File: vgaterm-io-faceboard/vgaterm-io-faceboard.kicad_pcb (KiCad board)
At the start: 2 copper layers, 37.6 x 19.1 mm, 8 parts, among them J1 Conn_01x02, J2 USB_B_Micro UART, J3 Conn_01x04, J4 Conn_01x04

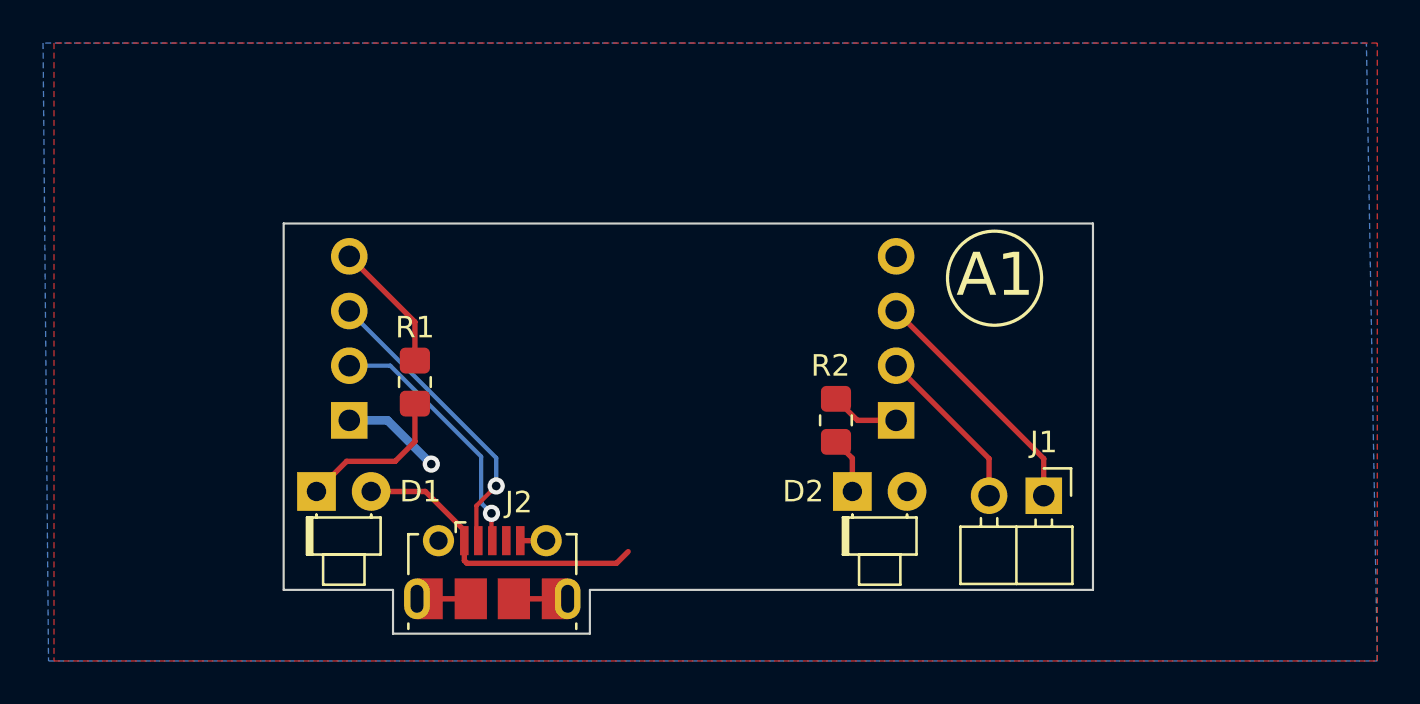
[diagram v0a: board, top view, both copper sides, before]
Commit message: updating timing board hsync vsync delay
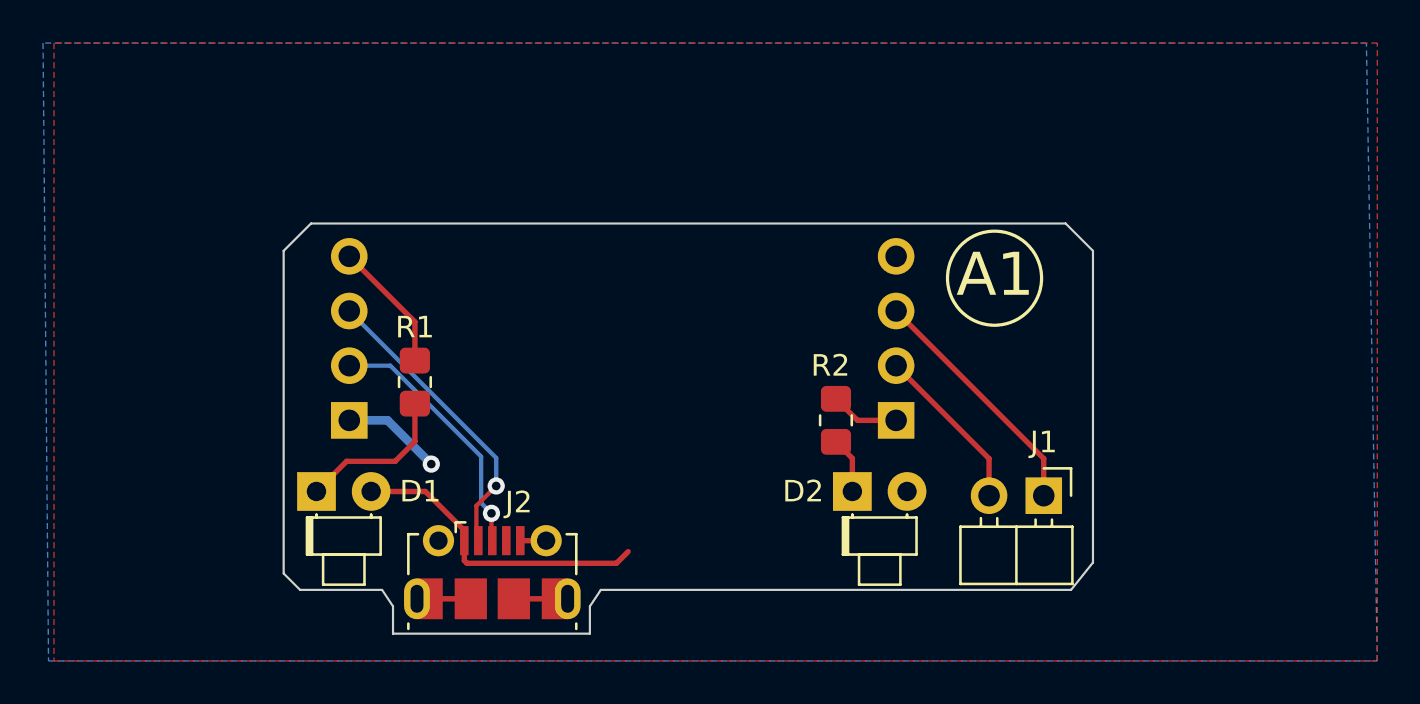
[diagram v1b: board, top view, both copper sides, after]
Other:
- outline, holes or cut-outs redrawn
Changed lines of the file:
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@@
   (gr_line (start 91.186 80.01) (end 82.042 80.01)
     (stroke (width 0.1) (type default)) (layer "Edge.Cuts"))
-  (gr_line (start 82.042 80.01) (end 82.042 77.978)
+  (gr_line (start 76.962 62.23) (end 78.232 60.96)
     (stroke (width 0.1) (type default)) (layer "Edge.Cuts"))
-  (gr_line (start 82.042 77.978) (end 76.962 77.978)
+  (gr_line (start 114.554 62.23) (end 113.284 60.96)
     (stroke (width 0.1) (type default)) (layer "Edge.Cuts"))
-  (gr_line (start 114.554 60.96) (end 114.554 77.978)
+  (gr_line (start 82.042 80.01) (end 82.042 78.74)
     (stroke (width 0.1) (type default)) (layer "Edge.Cuts"))
-  (gr_line (start 76.962 77.978) (end 76.962 60.96)
+  (gr_line (start 91.186 78.74) (end 91.694 77.978)
     (stroke (width 0.1) (type default)) (layer "Edge.Cuts"))
-  (gr_line (start 91.186 77.978) (end 91.186 80.01)
+  (gr_line (start 81.534 77.978) (end 82.042 78.74)
     (stroke (width 0.1) (type default)) (layer "Edge.Cuts"))
-  (gr_line (start 114.554 77.978) (end 91.186 77.978)
+  (gr_line (start 81.534 77.978) (end 77.724 77.978)
     (stroke (width 0.1) (type default)) (layer "Edge.Cuts"))
-  (gr_line (start 76.962 60.96) (end 114.554 60.96)
+  (gr_line (start 77.724 77.978) (end 76.962 77.216)
+    (stroke (width 0.1) (type default)) (layer "Edge.Cuts"))
+  (gr_line (start 114.554 62.23) (end 114.554 76.708)
+    (stroke (width 0.1) (type default)) (layer "Edge.Cuts"))
+  (gr_line (start 76.962 77.216) (end 76.962 62.23)
+    (stroke (width 0.1) (type default)) (layer "Edge.Cuts"))
+  (gr_line (start 113.538 77.978) (end 114.554 76.708)
+    (stroke (width 0.1) (type default)) (layer "Edge.Cuts"))
+  (gr_line (start 91.186 78.74) (end 91.186 80.01)
+    (stroke (width 0.1) (type default)) (layer "Edge.Cuts"))
+  (gr_line (start 113.538 77.978) (end 91.694 77.978)
+    (stroke (width 0.1) (type default)) (layer "Edge.Cuts"))
+  (gr_line (start 78.232 60.96) (end 113.284 60.96)
     (stroke (width 0.1) (type default)) (layer "Edge.Cuts"))
   (gr_text "A1" (at 108.204 64.516) (layer "F.SilkS")

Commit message: current boards
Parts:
- added C1: C_Small, Capacitor_SMD:C_0805_2012Metric_Pad1.18x1.45mm_HandSolder, B.Cu at (87.9, 72.4)
- added C2: C_Small, Capacitor_SMD:C_0805_2012Metric_Pad1.18x1.45mm_HandSolder, F.Cu at (89.2, 65.3)
- added C3: C_Small, Capacitor_SMD:C_0805_2012Metric_Pad1.18x1.45mm_HandSolder, B.Cu at (96.5, 64.5)
- added R10: R, Resistor_SMD:R_0805_2012Metric_Pad1.20x1.40mm_HandSolder, F.Cu at (108.9, 65.9)
- added R3: 4.7k, Resistor_SMD:R_0805_2012Metric_Pad1.20x1.40mm_HandSolder, F.Cu at (84.1, 71.9)
- added R4: 27, Resistor_SMD:R_0805_2012Metric_Pad1.20x1.40mm_HandSolder, F.Cu at (90.2, 68.3)
- added R5: 27, Resistor_SMD:R_0805_2012Metric_Pad1.20x1.40mm_HandSolder, F.Cu at (90.2, 70.6)
- added R6: 10k, Resistor_SMD:R_0805_2012Metric_Pad1.20x1.40mm_HandSolder, F.Cu at (84.1, 67.6)
- added R7: R, Resistor_SMD:R_0805_2012Metric_Pad1.20x1.40mm_HandSolder, B.Cu at (85.6, 67.3)
- added R8: R, Resistor_SMD:R_0805_2012Metric_Pad1.20x1.40mm_HandSolder, B.Cu at (84.1, 65.8)
- added R9: R, Resistor_SMD:R_0805_2012Metric_Pad1.20x1.40mm_HandSolder, F.Cu at (110.4, 67.4)
- added U1: FT230XS, Package_SO:SSOP-16_3.9x4.9mm_P0.635mm, F.Cu at (96.0, 69.6)
- R1: moved to B.Cu
- moved R1 8.65 mm to (79.5, 76.2), turned to 0 degrees
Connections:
- J1 pad 1: /RXI_{0} -> /RXI_{1}
- J1 pad 2: /TXI_{0} -> /TXI_{1}
- J2 pad 1: VCC -> Net-(J2-VBUS)
- J3 pad 2: /D+ -> Net-(J3-Pin_2)
- J3 pad 3: /D- -> Net-(J3-Pin_3)
- J4 pad 1: /S_{1} -> GND
- J4 pad 2: /TXI_{0} -> Net-(J4-Pin_2)
- J4 pad 3: /RXI_{0} -> Net-(J4-Pin_3)
- J4 pad 4: GND -> /S_{1}
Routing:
- net VCC: track 19.0 -> 1.60 mm, vias 1 -> 0
- net /V_sense: track 0.00 -> 15.3 mm
- net /RXI_{1}: track 0.00 -> 10.4 mm
- net /3v3: track 0.00 -> 10.3 mm, vias 0 -> 3
- net /S_{0}: track 6.10 -> 15.8 mm
- net Net-(U1-USBDP): track 0.00 -> 9.53 mm
- net Net-(U1-USBDM): track 0.00 -> 8.91 mm
- net GND: track 6.20 -> 14.2 mm, vias 0 -> 4
- net Net-(J3-Pin_2): track 0.00 -> 7.40 mm
- net Net-(J4-Pin_2): track 0.00 -> 6.81 mm
- net Net-(U1-~{CTS}): track 0.00 -> 6.78 mm
- net /TXI_{1}: track 0.00 -> 5.53 mm
- net /S_{1}: track 3.21 -> 7.78 mm
- net Net-(D1-K): track 7.29 -> 2.79 mm
- net /TXI_{0}: track 7.83 -> 11.9 mm, vias 0 -> 1
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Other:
- board text added: "GND"
- board text added: "Rx"
- board text added: "S1"
- board text added: "Tx"
